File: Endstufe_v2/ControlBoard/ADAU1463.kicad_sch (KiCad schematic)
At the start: 39 parts, among them J10 DNP, J11 DNP, J12 DNP, U7 W25Q128JVS, U8 ADAU1463WBCPZ300, U9 ZPLR135_T8, Y2 24.576Mhz

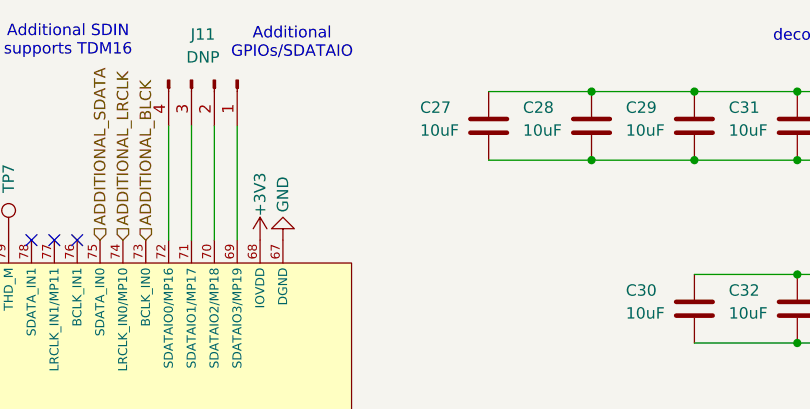
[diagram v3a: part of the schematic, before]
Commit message: Rough layout of components
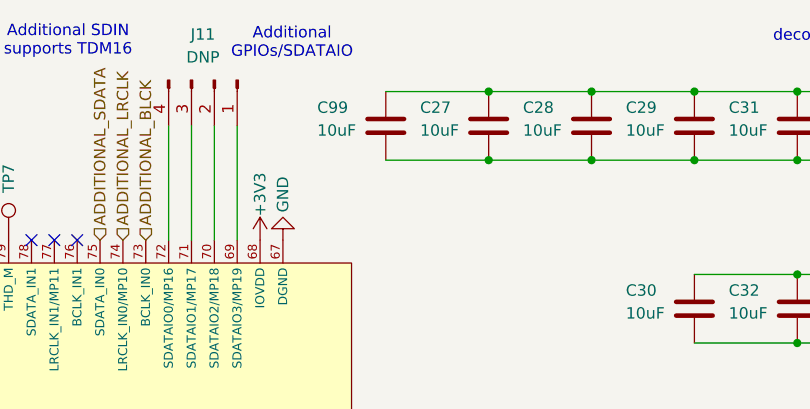
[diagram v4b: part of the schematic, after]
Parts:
- added C99: 10uF, Endstufe:C_0402_1005Metric, symbol Endstufe:C
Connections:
- net +3V3: now also C99.2
- net GND: now also C99.1
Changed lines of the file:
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@@
 	)
 	(junction
+		(at 196.85 38.1)
+		(diameter 0)
+		(color 0 0 0 0)
+	)
+	(junction
 		(at 231.14 30.48)
 		(diameter 0)
@@
 	)
 	(junction
+		(at 196.85 30.48)
+		(diameter 0)
+		(color 0 0 0 0)
+	)
+	(junction
 		(at 93.98 110.49)
 		(diameter 0)
@@
 	(wire
 		(pts
+			(xy 185.42 38.1) (xy 196.85 38.1)
+		)
+		(stroke
+			(width 0)
+			(type default)
+		)
+	)
+	(wire
+		(pts
 			(xy 39.37 93.98) (xy 39.37 95.25)
 		)
@@
 	(wire
 		(pts
+			(xy 185.42 30.48) (xy 196.85 30.48)
+		)
+		(stroke
+			(width 0)
+			(type default)
+		)
+	)
+	(wire
+		(pts
 			(xy 208.28 38.1) (xy 219.71 38.1)
 		)
@@
 					(unit 1)
 				)
+			)
+		)
+	)
+	(symbol
+		(lib_id "Endstufe:C")
+		(at 185.42 34.29 0)
+		(unit 1)
+		(exclude_from_sim no)
+		(in_bom yes)
+		(on_board yes)
+		(dnp no)
+		(property "Reference" "C99"
+			(at 177.8 32.258 0)
+			(effects
+				(font
+					(size 1.27 1.27)
+				)
+				(justify left)
+			)
+		)
+		(property "Value" "10uF"
+			(at 177.8 34.798 0)
+			(effects
+				(font
+					(size 1.27 1.27)
+				)
+				(justify left)
+			)
+		)
+		(property "Footprint" "Endstufe:C_0402_1005Metric"
+			(at 186.3852 38.1 0)
+			(effects
+				(font
+					(size 1.27 1.27)
+				)
+				(hide yes)
+			)
+		)
+		(property "Datasheet" "~"
+			(at 185.42 34.29 0)
+			(effects
+				(font
+					(size 1.27 1.27)
+				)
+				(hide yes)
+			)
+		)
+		(property "Description" "Unpolarized capacitor"
+			(at 185.42 34.29 0)
+			(effects
+				(font
+					(size 1.27 1.27)
+				)
+				(hide yes)
+			)
+		)
+		(property "LCSC Part #" "C15525"
+			(at 185.42 34.29 0)
+			(effects
+				(font
+					(size 1.27 1.27)
+				)
+				(hide yes)
+			)
+		)
+		(pin "1"
+		)
+		(pin "2"
+		)
+		(instances
+			(project "ControlBoard"
+				(path "/4f887f51-77c1-41d4-a3eb-45d362caffe1/70b67e3d-1dd9-4820-9634-6ce668eb2a07"
+					(reference "C99")
+					(unit 1)
+				)
